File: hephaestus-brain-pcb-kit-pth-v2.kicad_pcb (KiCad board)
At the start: 2 copper layers, 50.8 x 59.7 mm, 20 parts, among them J1 Barrel_Jack, J2 ItsyBitsy, J3 ItsyBitsy, J4 Conn_01x03_Male, J5 Conn_01x03_Male, J6 Conn_01x03_Male, J7 Conn_01x03_Male, J8 Conn_01x03_Male, SW1 SW_SPDT, SW2 SW_SPST, SW3 SW_SPST, U1 74126

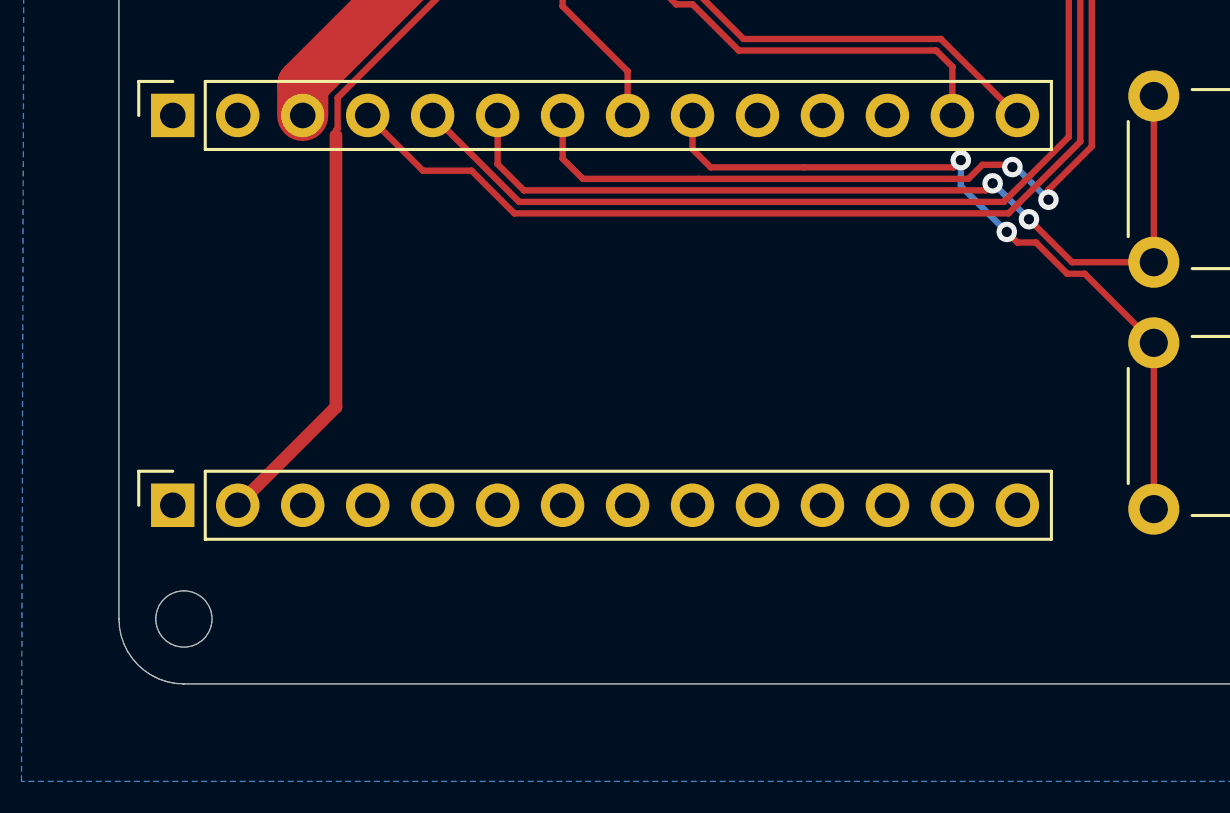
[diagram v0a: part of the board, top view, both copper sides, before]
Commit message: Updated silkscreen
* added QR code
* added board name, rev, author.
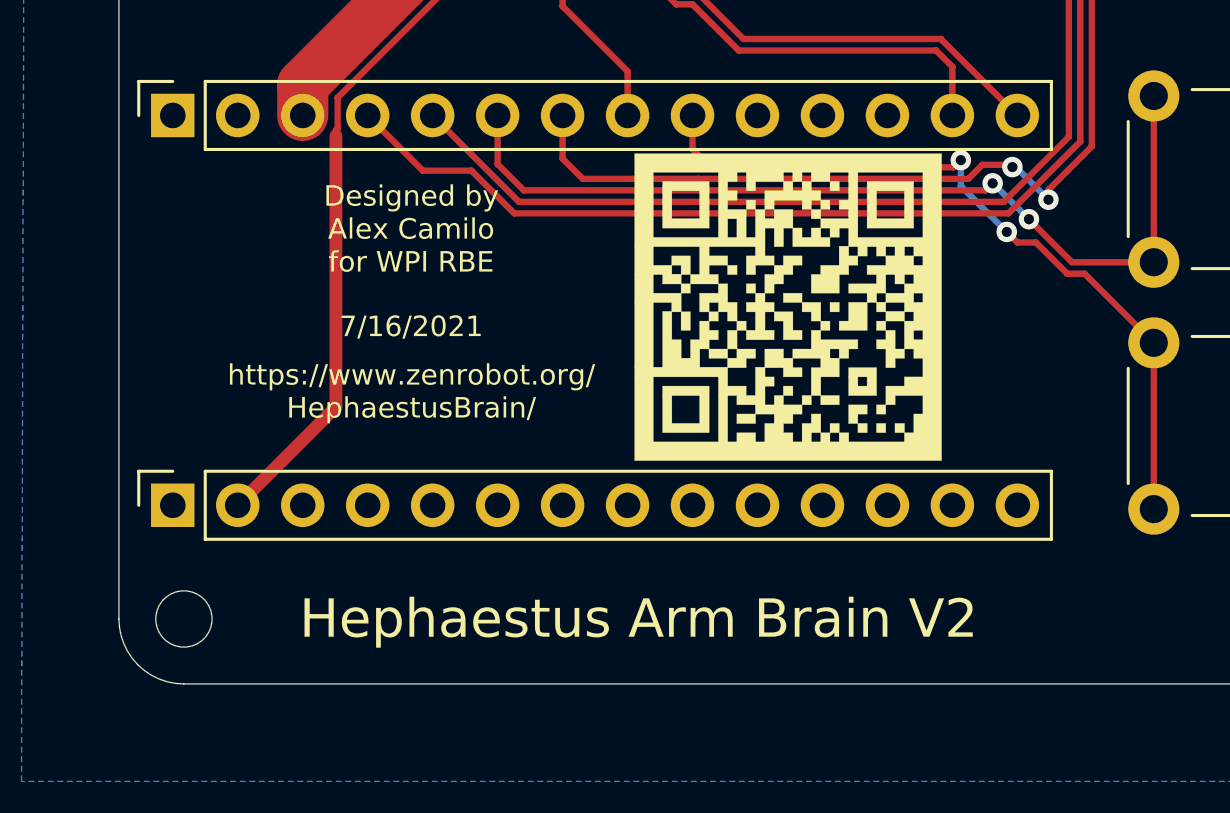
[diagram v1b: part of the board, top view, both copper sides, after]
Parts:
- added Ref**: Val**, qrcode:QRCode, F.Cu at (229.4, 99.6)
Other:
- board text added: "7/16/2021"
- board text added: "Designed by Alex Camilo for WPI RBE"
- board text added: "Hephaestus Arm Brain V2"
- board text added: "https://www.zenrobot.org/ HephaestusBrain/"
